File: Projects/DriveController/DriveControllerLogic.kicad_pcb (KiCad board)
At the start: 2 copper layers, 70 parts, among them J1 HPCE_40-24, J2 ISP_Header, Q1 PSMN1R0, Q2 PSMN1R0, Q3 PSMN1R0, Q4 PSMN1R0, Q5 PSMN1R0, Q6 PSMN1R0, Q7 PSMN1R0, Q8 BC817-40, U1 ATMega32M1, U2 MCP2562, U3 ATA6844, U4 ACS710

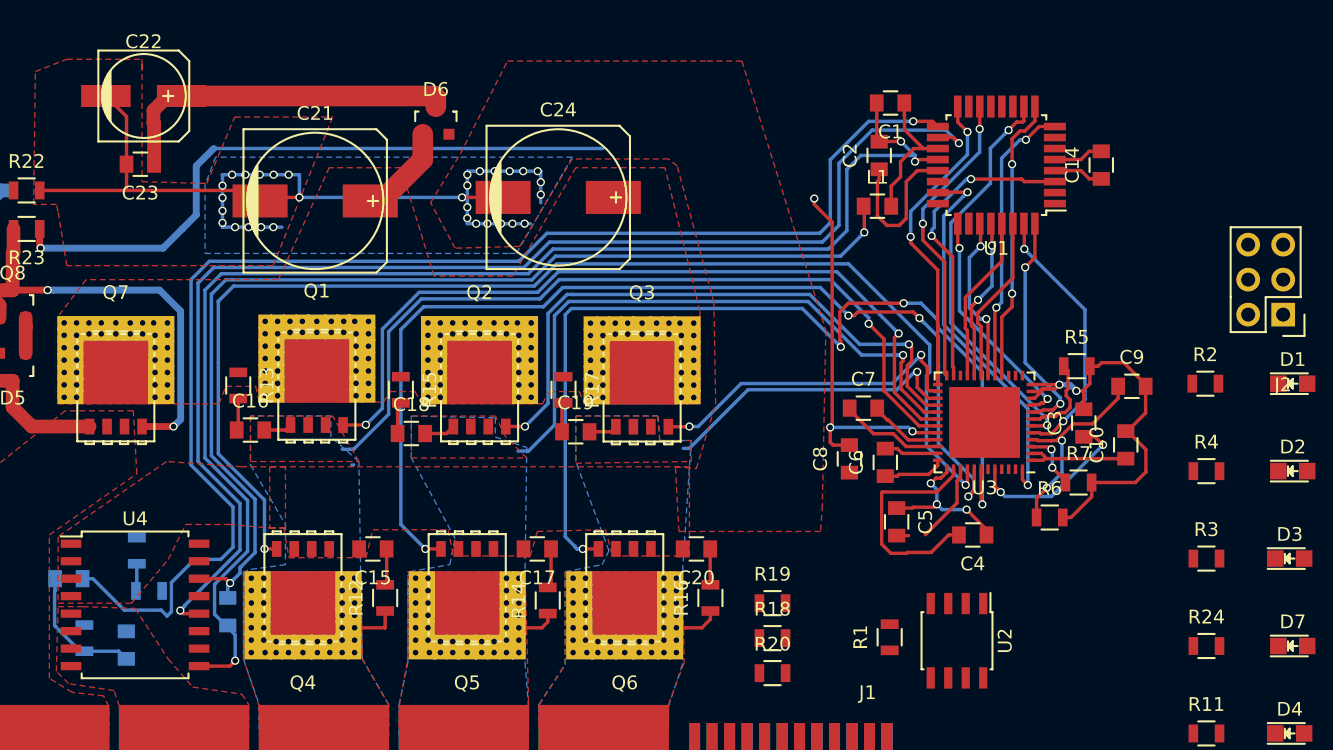
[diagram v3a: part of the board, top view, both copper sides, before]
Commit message: Optimizing logic traces
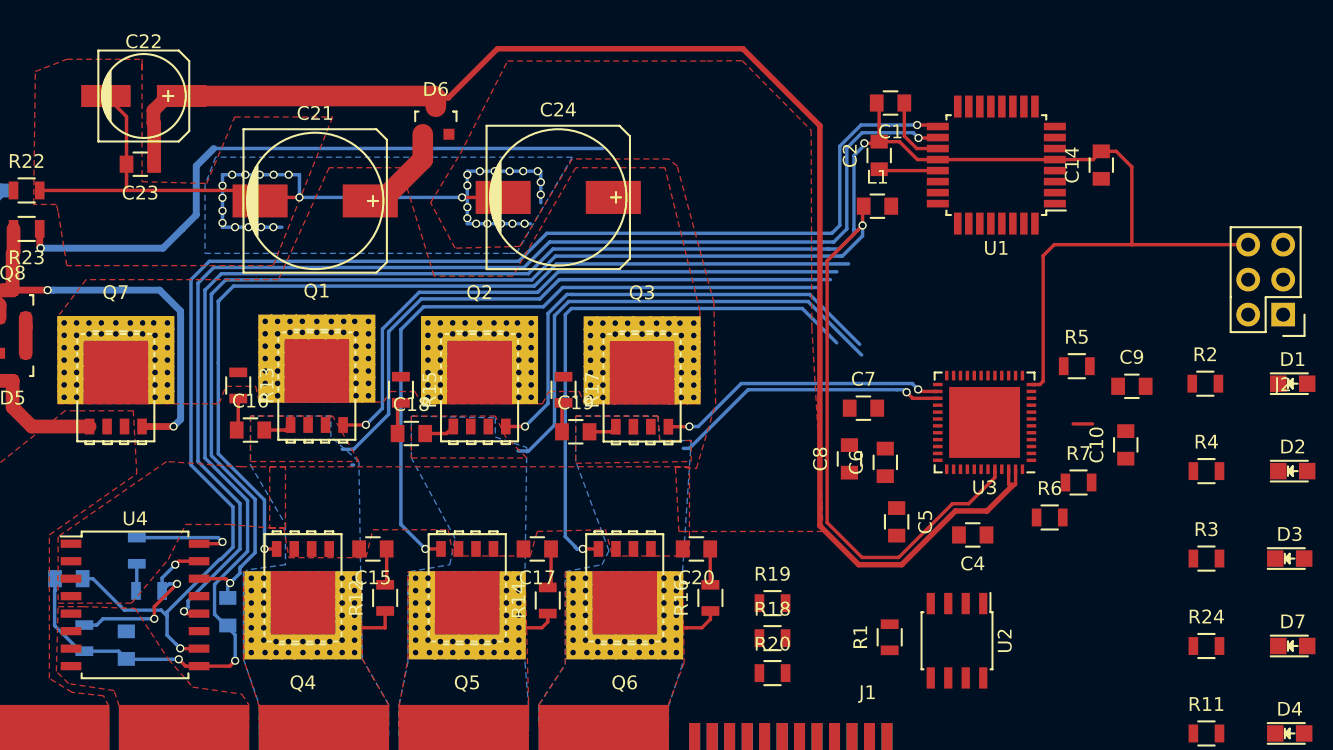
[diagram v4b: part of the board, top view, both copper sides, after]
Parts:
- removed C3: 2.2uF, Capacitors_SMD:C_0805
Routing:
- net /DriveControllerPower/VBAT: track 25.6 -> 106.6 mm
- net /WD: track 29.7 -> 0.00 mm, vias 2 -> 0
- net /DriveControllerPower/L3: track 68.1 -> 39.9 mm, vias 4 -> 1
- net /NCOAST: track 28.0 -> 0.00 mm, vias 2 -> 0
- net /DriveControllerPower/CPOUT: track 75.1 -> 47.3 mm, vias 4 -> 1
- net /DriveControllerPower/L2: track 75.4 -> 49.5 mm, vias 4 -> 1
- net /DG3: track 23.0 -> 0.00 mm, vias 2 -> 0
- net /5V0: track 94.1 -> 116.8 mm, vias 4 -> 2
- net /DG1: track 22.5 -> 0.00 mm, vias 2 -> 0
- net /DG2: track 22.0 -> 0.00 mm, vias 2 -> 0
- net /DriveControllerPower/L1: track 88.2 -> 67.2 mm, vias 2 -> 1
- net /IH3: track 20.8 -> 0.00 mm, vias 2 -> 0
- net /IL3: track 20.7 -> 0.00 mm, vias 2 -> 0
- net /NRESET: track 19.6 -> 0.00 mm, vias 2 -> 0
- net /SCREF: track 16.8 -> 0.00 mm, vias 2 -> 0
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
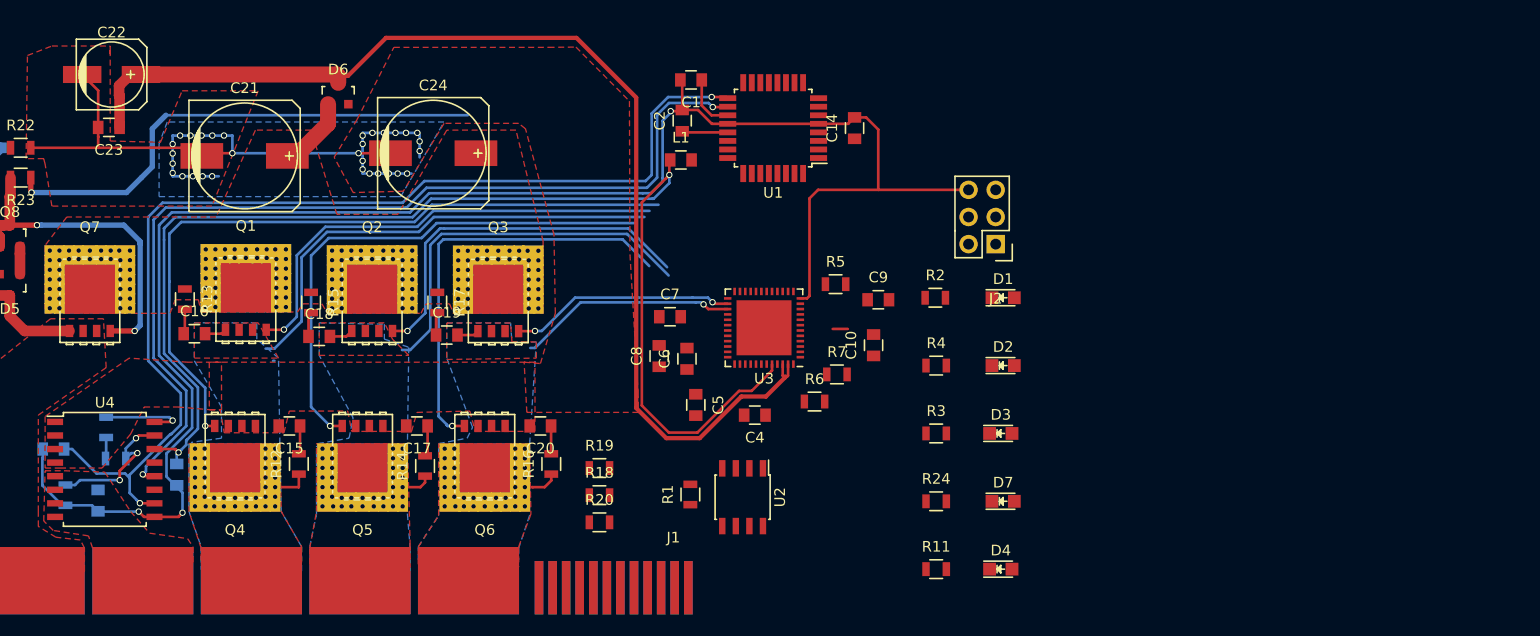
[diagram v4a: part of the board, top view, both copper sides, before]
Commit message: Lots of good progress on routing drive PCB
just a few traces and organization left
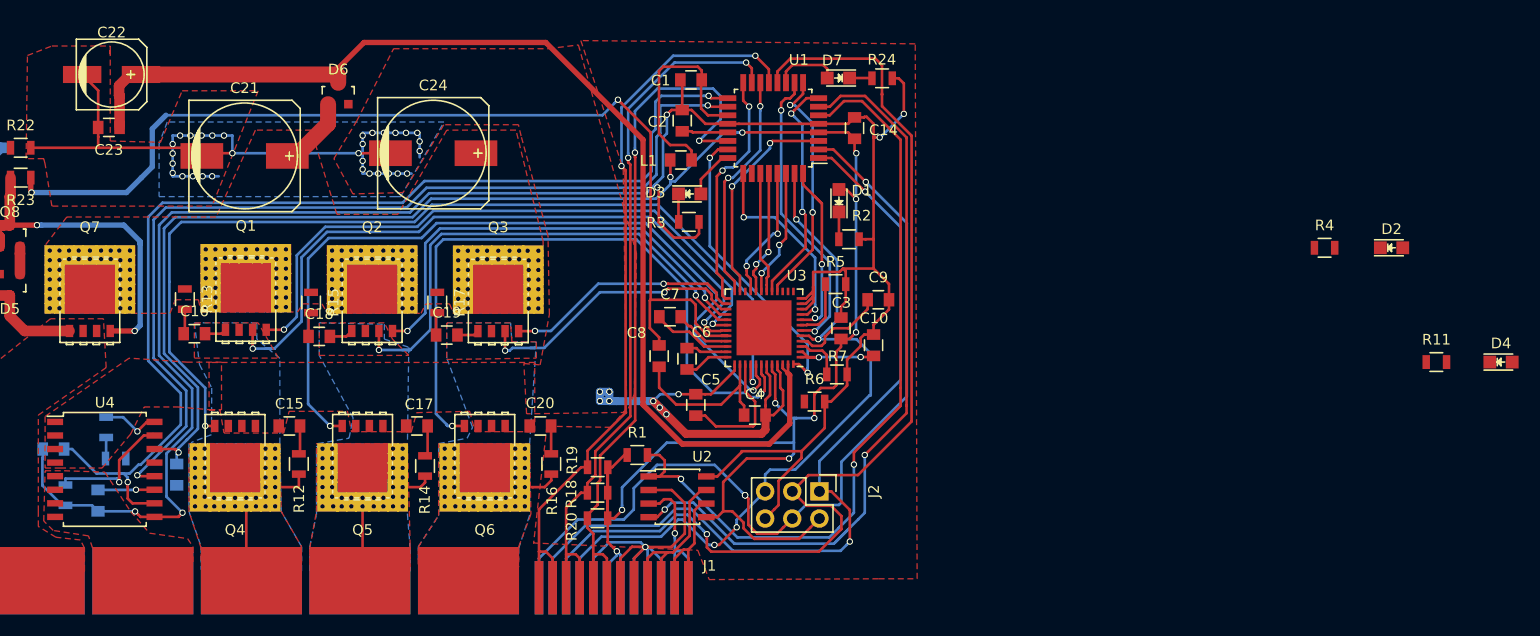
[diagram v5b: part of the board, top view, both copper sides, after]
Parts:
- added C3: 2.2uF, Capacitors_SMD:C_0805, F.Cu at (177.1, 122.4)
- moved D4 50.7 mm to (238.9, 125.6)
- moved R11 50.7 mm to (232.8, 125.6)
- moved D7 42.5 mm to (176.9, 99.0), turned to 180 degrees
- moved R24 39.9 mm to (180.9, 99.0)
- moved D2 38.0 mm to (228.6, 114.9)
- moved R4 38.0 mm to (222.4, 114.9)
- moved D3 36.7 mm to (162.9, 109.9)
- moved R3 30.5 mm to (162.9, 112.5)
- moved J2 28.4 mm to (175.1, 137.7), turned to 270 degrees
- moved D1 17.8 mm to (176.9, 110.5), turned to 90 degrees
- moved R2 9.76 mm to (177.9, 114.1)
- moved R1 6.19 mm to (158.0, 134.3), turned to 0 degrees
- moved U2 6.10 mm to (161.8, 138.2), turned to 0 degrees
- moved R20 0.42 mm to (154.3, 140.2), turned to 180 degrees
- moved R18 0.29 mm to (154.3, 137.8), turned to 180 degrees
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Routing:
- net /LGND: track 158.0 -> 258.8 mm, vias 3 -> 7
- net /SCK: track 0.00 -> 100.1 mm, vias 0 -> 1
- net /5V0: track 116.8 -> 207.5 mm, vias 2 -> 11
- net /MOSI: track 0.00 -> 81.0 mm, vias 0 -> 3
- net /MISO: track 0.00 -> 79.2 mm, vias 0 -> 2
- net /TXCAN: track 0.00 -> 73.9 mm, vias 0 -> 2
- net /RXCAN: track 0.00 -> 72.2 mm, vias 0 -> 2
- net /HA1: track 0.00 -> 70.7 mm, vias 0 -> 2
- net /NRESET: track 0.00 -> 68.7 mm, vias 0 -> 4
- net /HA3: track 0.00 -> 67.7 mm, vias 0 -> 2
- net /HA2: track 0.00 -> 66.9 mm, vias 0 -> 2
- net /DriveControllerPower/CPOUT: track 47.3 -> 96.9 mm, vias 1 -> 2
- net /DriveControllerPower/PGND: track 74.7 -> 118.0 mm, vias 31 -> 39
- net /WD: track 0.00 -> 27.9 mm, vias 0 -> 2
- net /DriveControllerPower/U: track 49.6 -> 77.2 mm, vias 0 -> 2
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- added copper zone on F.Cu, net /LGND

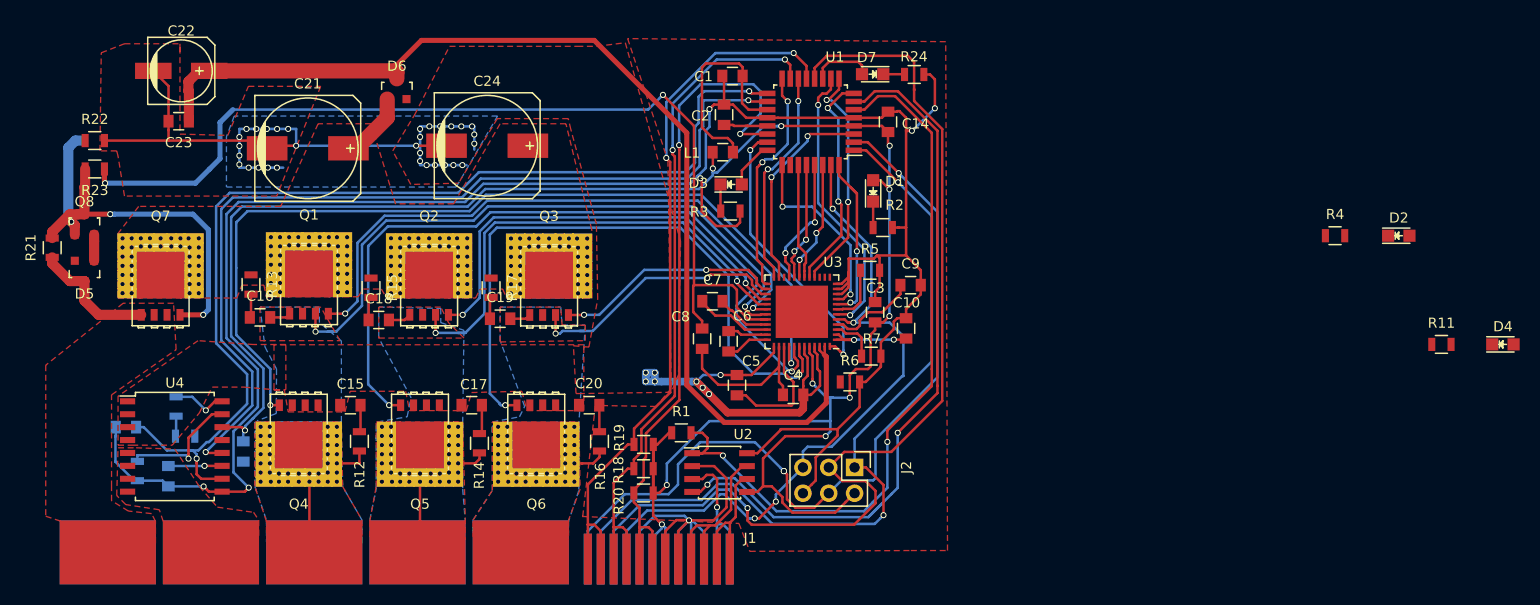
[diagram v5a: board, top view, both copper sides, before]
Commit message: More PCB layout cleaning for Drive PCB
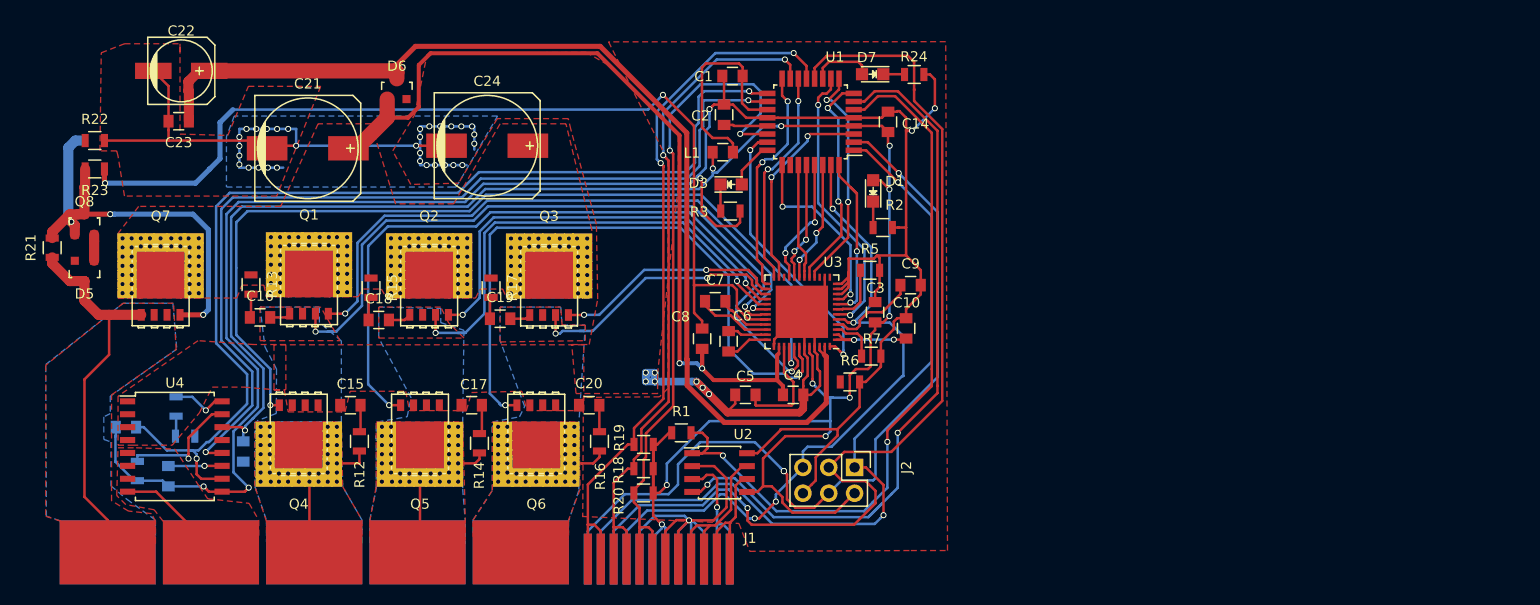
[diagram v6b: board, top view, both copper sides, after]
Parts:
- removed D2: LED_COAST, LEDs:LED-0805
- removed D4: LED_IOK, LEDs:LED-0805
- removed R11, R4: 1k, Resistors_SMD:R_0805
- moved C5 1.26 mm to (164.3, 130.6), turned to 0 degrees
- moved C7 0.27 mm to (161.4, 121.3)
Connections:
- U1 pad 26: /I_OK -> (no net)
- U3 pad 49: (no net) -> /DriveControllerPower/PGND
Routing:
- net /DriveControllerPower/PBAT: track 23.1 -> 85.4 mm, vias 0 -> 2
- net /DriveControllerPower/PGND: track 118.0 -> 158.4 mm, vias 39 -> 38
- net /DriveControllerPower/VSUPPLY: track 12.6 -> 37.9 mm
- net Net-(C5-Pad2): track 12.1 -> 10.8 mm
- added copper zone on B.Cu, net /DriveControllerPower/VSUPPLY

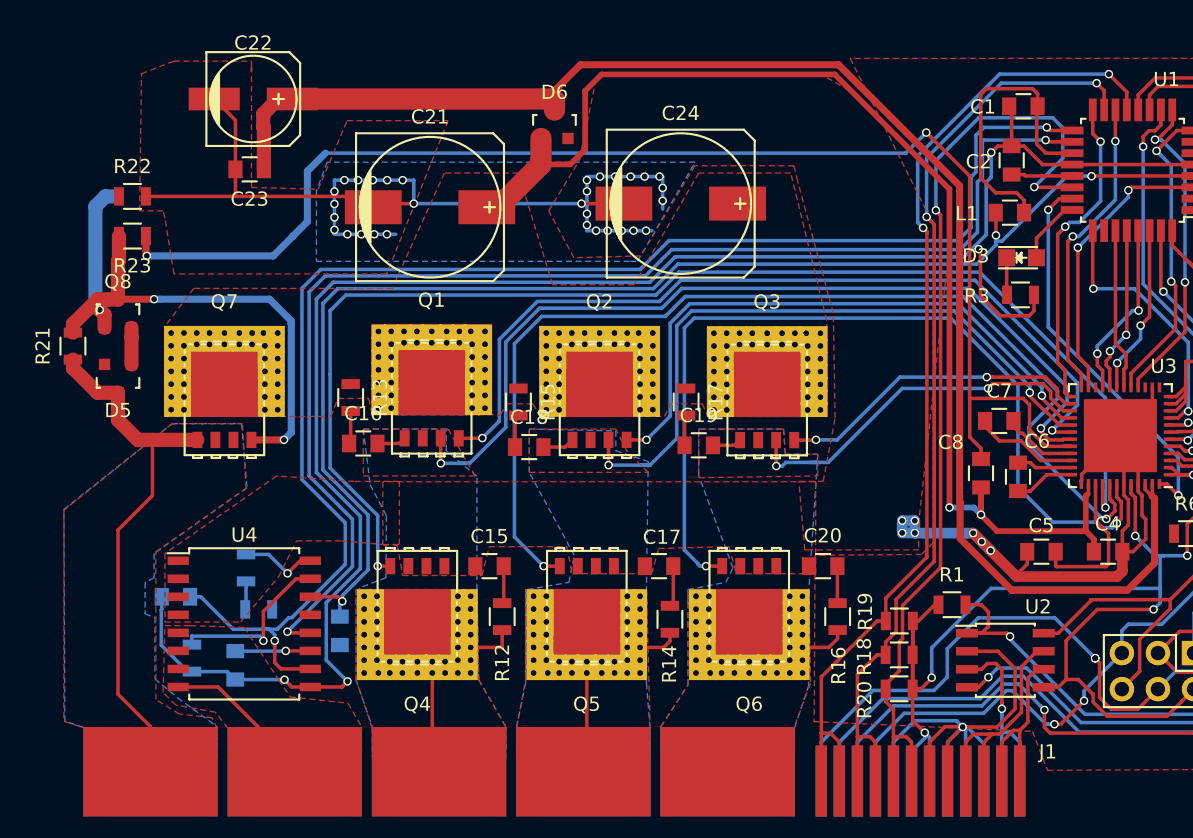
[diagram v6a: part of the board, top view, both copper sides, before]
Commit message: Added reference designs, work on Pi Board and (deprecated) motor control board
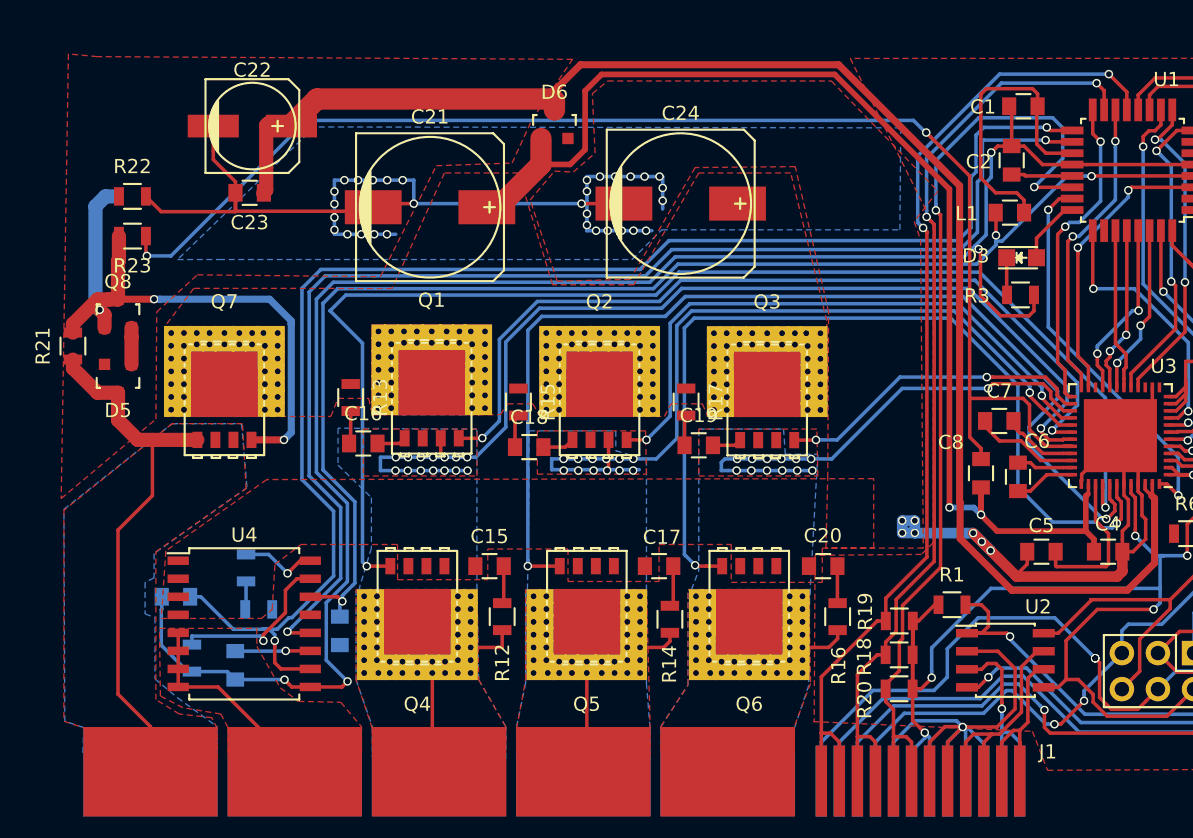
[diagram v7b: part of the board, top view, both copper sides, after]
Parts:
- moved C22 1.91 mm to (108.8, 100.6)
- moved C23 1.65 mm to (108.6, 105.3)
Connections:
- C21 pad 2: /DriveControllerPower/PGND -> /DriveControllerPower/POUT
- C22 pad 2: /DriveControllerPower/PGND -> /DriveControllerPower/POUT
- C23 pad 2: /DriveControllerPower/PGND -> /DriveControllerPower/POUT
- C24 pad 2: /DriveControllerPower/PGND -> /DriveControllerPower/POUT
- C4 pad 1: /DriveControllerPower/PGND -> /DriveControllerPower/POUT
- C5 pad 1: /DriveControllerPower/PGND -> /DriveControllerPower/POUT
- J1 pad 33: /DriveControllerPower/PGND -> /PGND
- J1 pad 5: /DriveControllerPower/PGND -> /PGND
- R22 pad 2: /DriveControllerPower/PGND -> /DriveControllerPower/POUT
- U3 pad 14: /DriveControllerPower/PGND -> /DriveControllerPower/POUT
- U3 pad 37: /DriveControllerPower/PGND -> /DriveControllerPower/POUT
- U3 pad 43: /DriveControllerPower/PGND -> /DriveControllerPower/POUT
- U3 pad 45: /DriveControllerPower/PGND -> /DriveControllerPower/POUT
- U3 pad 49: /DriveControllerPower/PGND -> /DriveControllerPower/POUT
- U4 pad 5: /DriveControllerPower/PGND -> /PGND
- U4 pad 6: /DriveControllerPower/PGND -> /PGND
- U4 pad 7: /DriveControllerPower/PGND -> /PGND
- U4 pad 8: /DriveControllerPower/PGND -> /PGND
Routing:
- net /DriveControllerPower/PGND: track 158.4 -> 0.00 mm, vias 38 -> 0
- net /DriveControllerPower/POUT: track 0.00 -> 147.8 mm, vias 0 -> 38
- net /PGND: track 0.00 -> 14.8 mm
- net /DriveControllerPower/V: track 60.2 -> 70.6 mm, vias 2 -> 13
- net /DriveControllerPower/U: track 77.2 -> 87.4 mm, vias 2 -> 15
- net /DriveControllerPower/W: track 32.0 -> 40.4 mm, vias 2 -> 13
- net /DriveControllerPower/CPOUT: track 96.8 -> 95.6 mm
- net /DriveControllerPower/VBAT: track 106.7 -> 107.9 mm
- net /5V0: track 207.5 -> 206.8 mm
- net /LGND: track 258.8 -> 258.1 mm
- net /ISENSEP: track 90.5 -> 89.8 mm
- net /ISENSEN: track 102.7 -> 102.1 mm
- added copper zone on B.Cu, net /DriveControllerPower/POUT
- removed copper zone on B.Cu, net /DriveControllerPower/PGND
